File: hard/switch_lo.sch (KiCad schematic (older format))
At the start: 4 parts, among them M66 IRLML0030TRPBF

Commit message: layout progress. todo: led drivers
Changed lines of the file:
@@
 AR Path="/6053C67A/DAE5EF41/6879FA6E" Ref="M96"  Part="1"
 AR Path="/6053C67A/DAE5EF45/6879FA6E" Ref="M97"  Part="1"
-F 0 "M82" H 6078 4300 50  0000 L CNN
+F 0 "M97" H 6078 4300 50  0000 L CNN
 F 1 "IRLML0030TRPBF" H 6078 4255 50  0001 L CNN
 F 2 "Package_TO_SOT_SMD:SOT-23" H 6750 4300 50  0001 C CNN
@@
 AR Path="/6053C67A/DAE5EF41/6879FA74" Ref="R199"  Part="1"
 AR Path="/6053C67A/DAE5EF45/6879FA74" Ref="R202"  Part="1"
-F 0 "R157" H 5720 4546 50  0000 L CNN
+F 0 "R202" H 5720 4546 50  0000 L CNN
 F 1 "470K" H 5720 4455 50  0000 L CNN
 F 2 "Resistor_SMD:R_0402_1005Metric" V 5580 4500 50  0001 C CNN
@@
 AR Path="/6053C67A/DAE5EF41/6879FA7A" Ref="R198"  Part="1"
 AR Path="/6053C67A/DAE5EF45/6879FA7A" Ref="R201"  Part="1"
-F 0 "R156" V 5243 4300 50  0000 C CNN
+F 0 "R201" V 5243 4300 50  0000 C CNN
 F 1 "1K8" V 5334 4300 50  0000 C CNN
 F 2 "Resistor_SMD:R_0402_1005Metric" V 5380 4300 50  0001 C CNN
@@
 AR Path="/6053C67A/DAE5EF41/6879FA80" Ref="#PWR0183"  Part="1"
 AR Path="/6053C67A/DAE5EF45/6879FA80" Ref="#PWR0185"  Part="1"
-F 0 "#PWR0155" H 5650 4450 50  0001 C CNN
+F 0 "#PWR0185" H 5650 4450 50  0001 C CNN
 F 1 "GND" H 5655 4527 50  0000 C CNN
 F 2 "" H 5650 4700 50  0001 C CNN
@@
 AR Path="/6053C67A/DAE5EF41/6879FA89" Ref="#PWR0184"  Part="1"
 AR Path="/6053C67A/DAE5EF45/6879FA89" Ref="#PWR0186"  Part="1"
-F 0 "#PWR0156" H 6000 4450 50  0001 C CNN
+F 0 "#PWR0186" H 6000 4450 50  0001 C CNN
 F 1 "GND" H 6005 4527 50  0000 C CNN
 F 2 "" H 6000 4700 50  0001 C CNN
@@
 AR Path="/6053C67A/DAE5EF41/6879FB77" Ref="R197"  Part="1"
 AR Path="/6053C67A/DAE5EF45/6879FB77" Ref="R200"  Part="1"
-F 0 "R155" H 6070 3896 50  0000 L CNN
+F 0 "R200" H 6070 3896 50  0000 L CNN
 F 1 "0R" H 6070 3805 50  0000 L CNN
 F 2 "Resistor_SMD:R_1210_3225Metric" V 5930 3850 50  0001 C CNN

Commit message: layout progress
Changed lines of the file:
@@
 $Descr A4 11693 8268
 encoding utf-8
-Sheet 52 69
+Sheet 62 69
 Title ""
 Date ""
@@
 AR Path="/6053C67A/DAE5EF41/6879FA6E" Ref="M96"  Part="1"
 AR Path="/6053C67A/DAE5EF45/6879FA6E" Ref="M97"  Part="1"
-F 0 "M97" H 6078 4300 50  0000 L CNN
+F 0 "M92" H 6078 4300 50  0000 L CNN
 F 1 "IRLML0030TRPBF" H 6078 4255 50  0001 L CNN
 F 2 "Package_TO_SOT_SMD:SOT-23" H 6750 4300 50  0001 C CNN
@@
 AR Path="/6053C67A/DAE5EF41/6879FA74" Ref="R199"  Part="1"
 AR Path="/6053C67A/DAE5EF45/6879FA74" Ref="R202"  Part="1"
-F 0 "R202" H 5720 4546 50  0000 L CNN
+F 0 "R187" H 5720 4546 50  0000 L CNN
 F 1 "470K" H 5720 4455 50  0000 L CNN
 F 2 "Resistor_SMD:R_0402_1005Metric" V 5580 4500 50  0001 C CNN
@@
 AR Path="/6053C67A/DAE5EF41/6879FA7A" Ref="R198"  Part="1"
 AR Path="/6053C67A/DAE5EF45/6879FA7A" Ref="R201"  Part="1"
-F 0 "R201" V 5243 4300 50  0000 C CNN
+F 0 "R186" V 5243 4300 50  0000 C CNN
 F 1 "1K8" V 5334 4300 50  0000 C CNN
 F 2 "Resistor_SMD:R_0402_1005Metric" V 5380 4300 50  0001 C CNN
@@
 AR Path="/6053C67A/DAE5EF41/6879FB77" Ref="R197"  Part="1"
 AR Path="/6053C67A/DAE5EF45/6879FB77" Ref="R200"  Part="1"
-F 0 "R200" H 6070 3896 50  0000 L CNN
+F 0 "R185" H 6070 3896 50  0000 L CNN
 F 1 "0R" H 6070 3805 50  0000 L CNN
 F 2 "Resistor_SMD:R_1210_3225Metric" V 5930 3850 50  0001 C CNN

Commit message: release candidate. ready for review by @lukekaese
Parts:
- R107: value 0R -> 120R
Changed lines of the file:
@@
 $Descr A4 11693 8268
 encoding utf-8
-Sheet 62 69
-Title ""
-Date ""
-Rev ""
-Comp ""
+Sheet 67 70
+Title "LED Matrix V3"
+Date "2021-03-23"
+Rev "0"
+Comp "F2A"
 Comment1 ""
 Comment2 ""
@@
 AR Path="/6053C67A/DAE5EF41/6879FA6E" Ref="M96"  Part="1"
 AR Path="/6053C67A/DAE5EF45/6879FA6E" Ref="M97"  Part="1"
-F 0 "M92" H 6078 4300 50  0000 L CNN
+F 0 "M97" H 6078 4300 50  0000 L CNN
 F 1 "IRLML0030TRPBF" H 6078 4255 50  0001 L CNN
 F 2 "Package_TO_SOT_SMD:SOT-23" H 6750 4300 50  0001 C CNN
@@
 AR Path="/6053C67A/DAE5EF41/6879FA74" Ref="R199"  Part="1"
 AR Path="/6053C67A/DAE5EF45/6879FA74" Ref="R202"  Part="1"
-F 0 "R187" H 5720 4546 50  0000 L CNN
+F 0 "R202" H 5720 4546 50  0000 L CNN
 F 1 "470K" H 5720 4455 50  0000 L CNN
 F 2 "Resistor_SMD:R_0402_1005Metric" V 5580 4500 50  0001 C CNN
@@
 AR Path="/6053C67A/DAE5EF41/6879FA7A" Ref="R198"  Part="1"
 AR Path="/6053C67A/DAE5EF45/6879FA7A" Ref="R201"  Part="1"
-F 0 "R186" V 5243 4300 50  0000 C CNN
+F 0 "R201" V 5243 4300 50  0000 C CNN
 F 1 "1K8" V 5334 4300 50  0000 C CNN
 F 2 "Resistor_SMD:R_0402_1005Metric" V 5380 4300 50  0001 C CNN
@@
 AR Path="/6053C67A/DAE5EF41/6879FB77" Ref="R197"  Part="1"
 AR Path="/6053C67A/DAE5EF45/6879FB77" Ref="R200"  Part="1"
-F 0 "R185" H 6070 3896 50  0000 L CNN
-F 1 "0R" H 6070 3805 50  0000 L CNN
+F 0 "R200" H 6070 3896 50  0000 L CNN
+F 1 "120R" H 6070 3805 50  0000 L CNN
 F 2 "Resistor_SMD:R_1210_3225Metric" V 5930 3850 50  0001 C CNN
 F 3 "~" H 6000 3850 50  0001 C CNN

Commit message: attribute naming update
JLCPCB_Part_Number -> LCSC
DigiKey_Part_Number -> DigiKey
Mouser_Part_Number -> Mouser
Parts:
- M66: DigiKey (none) -> IRLML0030TRPBFCT-ND; DigiKey_Part_Number IRLML0030TRPBFCT-ND -> (none); JLCPCB_Part_Number C67272 -> (none); LCSC (none) -> C67272; Mouser (none) -> 942-IRLML0030TRPBF; Mouser_Part_Number 942-IRLML0030TRPBF -> (none)
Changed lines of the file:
@@
 F 2 "Package_TO_SOT_SMD:SOT-23" H 6750 4300 50  0001 C CNN
 F 3 "https://www.infineon.com/dgdl/irlml0030pbf.pdf?fileId=5546d462533600a401535664773825df" H 5950 4300 50  0001 C CNN
-F 4 "IRLML0030TRPBFCT-ND" H 6750 4300 50  0001 C CNN "DigiKey_Part_Number"
-F 5 "942-IRLML0030TRPBF" H 6750 4300 50  0001 C CNN "Mouser_Part_Number"
-F 6 "C67272" H 6350 4200 50  0001 C CNN "JLCPCB_Part_Number"
+F 4 "IRLML0030TRPBFCT-ND" H 6750 4300 50  0001 C CNN "DigiKey"
+F 5 "942-IRLML0030TRPBF" H 6750 4300 50  0001 C CNN "Mouser"
+F 6 "C67272" H 6350 4200 50  0001 C CNN "LCSC"
 F 7 "Infineon Technologies" H 6750 4300 50  0001 C CNN "MF"
 F 8 "IRLML0030TRPBF" H 6750 4300 50  0001 C CNN "MPN"

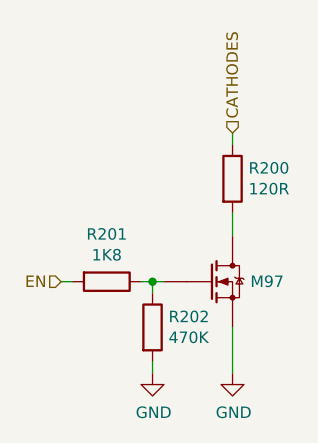
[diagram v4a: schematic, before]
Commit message: re-connect footprints
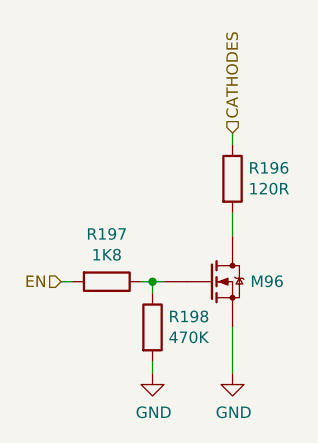
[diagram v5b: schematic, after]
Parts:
- renumbered M66 to M65, R107 to R103, R108 to R104, R109 to R105
